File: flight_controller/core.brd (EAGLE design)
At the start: 94 x 90 mm, 116 parts, among them J1 MOLEX-2POS, J10 MOLEX-2POS, J11 MOLEX-2POS, J12 MOLEX-2POS, J13 MOLEX-3POS, J14 MOLEX-3POS, J15 MOLEX-4POS, J16 MOLEX-3POS, J17 MOLEX-3POS, J18 MOLEX-3POS, J19 MOLEX-3POS, J2 MOLEX-2POS, J20 MOLEX-4POS, J3 MOLEX-2POS, J4 MOLEX-2POS, J5 MOLEX-2POS, J6 MOLEX-2POS, J7 MOLEX-2POS, J8 MOLEX-2POS, J9 MOLEX-2POS, Q1 MMBT2222A, Q14 MMBT2222A, Q15 MMBT2222A, Q16 MMBT2222A, Q17 MMBT2222A, Q3 MMBT2222A, Q4 MMBT2222A, Q9 MMBT2222A, U1 MPU-6000QFN-24, U2 MEAS-MS5611, U3 USD-SOCKETNEW, U4 STM32F405, U5 MIC5219 3.3V

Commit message: Replace XBee headers with SMD variant.
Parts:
- removed XB1: XBEE-PRO, maxstream:XBEE-PRO
- added U$1: XBEE-1B3, SparkFun-RF:XBEE-SMD
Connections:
- net 3.3V: now also U$1.1; no longer XB1.1
- net GND: now also U$1.10; no longer XB1.10
- net KILL: now also U$1.20; no longer XB1.20
- net RSSI: now also U$1.6; no longer XB1.6
- net RST: now also U$1.5; no longer XB1.5
- net UART6-RX: now also U$1.2; no longer XB1.2
- net UART6-TX: now also U$1.3; no longer XB1.3
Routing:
- net RSSI: track 27.9 -> 0.00 mm, vias 2 -> 0
- net RST: track 10.6 -> 0.00 mm
- net KILL: track 1.00 -> 0.00 mm
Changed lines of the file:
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@@
 </autorouter>
 <elements>
-<element name="XB1" library="maxstream" package="XBEE-PRO" value="XBEE-PRO" x="34.9" y="16.1" rot="R180">
-<attribute name="OC_NEWARK" value="42M2667" x="34.9" y="16.1" size="1.778" layer="27" rot="R180" display="off"/>
-<attribute name="MPN" value="XBP24-AWI-001" x="34.9" y="16.1" size="1.778" layer="27" rot="R180" display="off"/>
-<attribute name="MF" value="" x="34.9" y="16.1" size="1.778" layer="27" rot="R180" display="off"/>
-<attribute name="OC_FARNELL" value="1337916" x="34.9" y="16.1" size="1.778" layer="27" rot="R180" display="off"/>
-</element>
 <element name="U3" library="SparkFun-Connectors" package="MICRO-SD-SOCKET-PP" value="USD-SOCKETNEW" x="-0.5" y="-145.6">
 <attribute name="PROD_ID" value="CONN-07820" x="-0.5" y="-145.6" size="1.778" layer="27" display="off"/>
@@
 <element name="C16" library="SparkFun-Capacitors" package="0603-CAP" value="18pF" x="-187.5" y="-506.7">
 <attribute name="PROD_ID" value="CAP-08267" x="-187.5" y="-506.7" size="1.778" layer="27" display="off"/>
+</element>
+<element name="U$1" library="SparkFun-RF" package="XBEE-SMD" value="XBEE-1B3" x="-202.6" y="-501.9">
+<attribute name="PROD_ID" value="CONN-09042" x="-202.6" y="-501.9" size="1.778" layer="27" display="off"/>
 </element>
 </elements>
@@
 <via x="33" y="41" extent="1-16" drill="0.381"/>
 <wire x1="35.7" y1="36.5" x2="35.7" y2="36.6" width="0.8128" layer="1"/>
-<contactref element="XB1" pad="10"/>
 <contactref element="U4" pad="18"/>
 <contactref element="U4" pad="63"/>
@@
 <contactref element="C15" pad="2"/>
 <contactref element="C16" pad="2"/>
+<contactref element="U$1" pad="10"/>
 <wire x1="-127.4" y1="-372.6" x2="-136" y2="-372.6" width="0" layer="19" extent="1-1"/>
 <wire x1="-120.8" y1="-372.6" x2="-127.4" y2="-372.6" width="0" layer="19" extent="1-1"/>
@@
 <wire x1="-186.65" y1="-503.7" x2="-186.65" y2="-496.4" width="0" layer="19" extent="1-1"/>
 <wire x1="-186.65" y1="-506.7" x2="-186.65" y2="-503.7" width="0" layer="19" extent="1-1"/>
+<wire x1="-212.1" y1="-499.9" x2="-186.65" y2="-496.4" width="0" layer="19" extent="1-1"/>
 <wire x1="-36.2" y1="-212.723" x2="-41.25" y2="-287.7" width="0" layer="19" extent="1-1"/>
 <wire x1="-33.3" y1="-212.723" x2="-36.2" y2="-212.723" width="0" layer="19" extent="1-1"/>
@@
 <wire x1="-14.1" y1="-131.05" x2="-3.94" y2="-134.7" width="0" layer="19" extent="1-1"/>
 <wire x1="44.2" y1="2.1" x2="-0.95" y2="-132.05" width="0" layer="19" extent="1-1"/>
-<wire x1="45.9" y1="25.1" x2="44.2" y2="2.1" width="0" layer="19" extent="1-1"/>
-<wire x1="35.7" y1="36.5" x2="45.9" y2="25.1" width="0" layer="19" extent="1-1"/>
+<wire x1="35.7" y1="36.5" x2="44.2" y2="2.1" width="0" layer="19" extent="1-1"/>
 <wire x1="33" y1="41" x2="35.7" y2="36.6" width="0" layer="19" extent="1-1"/>
 <wire x1="31" y1="41" x2="33" y2="41" width="0" layer="19" extent="1-1"/>
@@
 </signal>
 <signal name="RST">
-<contactref element="XB1" pad="5"/>
-<wire x1="45.9" y1="15.1" x2="47.4" y2="15.1" width="0.254" layer="1"/>
-<wire x1="47.4" y1="15.1" x2="47.7" y2="14.8" width="0.254" layer="1"/>
-<wire x1="47.7" y1="14.8" x2="47.7" y2="10.2" width="0.254" layer="1"/>
-<wire x1="47.7" y1="10.2" x2="49.4" y2="8.5" width="0.254" layer="1"/>
-<wire x1="49.4" y1="8.5" x2="51.1" y2="8.5" width="0.254" layer="1"/>
 <contactref element="S1" pad="1"/>
 <contactref element="R8" pad="1"/>
 <contactref element="J20" pad="1"/>
+<contactref element="U$1" pad="5"/>
 <wire x1="-42.794" y1="-359.895" x2="-14.15" y2="-182.7" width="0" layer="19" extent="1-1"/>
 <wire x1="-183" y1="-382.5" x2="-42.794" y2="-359.895" width="0" layer="19" extent="1-1"/>
-<wire x1="49.4" y1="8.5" x2="-14.15" y2="-182.7" width="0" layer="19" extent="1-1"/>
+<wire x1="-215.1" y1="-489.9" x2="-183" y2="-382.5" width="0" layer="19" extent="1-1"/>
 </signal>
 <signal name="PA12">
@@
 </signal>
 <signal name="3.3V">
-<contactref element="XB1" pad="1"/>
 <contactref element="U4" pad="1"/>
 <contactref element="U4" pad="19"/>
@@
 <contactref element="U4" pad="64"/>
 <contactref element="C9" pad="1"/>
+<contactref element="U$1" pad="1"/>
 <wire x1="-138" y1="-372.6" x2="-129.4" y2="-372.6" width="0" layer="19" extent="1-1"/>
 <wire x1="-180.7138" y1="-413.9967" x2="-138" y2="-372.6" width="0" layer="19" extent="1-1"/>
@@
 <wire x1="-186.65" y1="-475.4" x2="-188.35" y2="-466.4" width="0" layer="19" extent="1-1"/>
 <wire x1="-186.65" y1="-478.4" x2="-186.65" y2="-475.4" width="0" layer="19" extent="1-1"/>
+<wire x1="-215.1" y1="-481.9" x2="-186.65" y2="-478.4" width="0" layer="19" extent="1-1"/>
 <wire x1="-41.35" y1="-358.1" x2="-129.4" y2="-372.6" width="0" layer="19" extent="1-1"/>
 <wire x1="-33.75" y1="-222.5" x2="-41.35" y2="-358.1" width="0" layer="19" extent="1-1"/>
@@
 <wire x1="-1.7" y1="-161.9" x2="-8.2" y2="-161.9" width="0" layer="19" extent="1-1"/>
 <wire x1="0.5" y1="-152.2" x2="-9.2" y2="-150" width="0" layer="19" extent="1-1"/>
-<wire x1="45.9" y1="7.1" x2="0.5" y2="-152.2" width="0" layer="19" extent="1-1"/>
 </signal>
 <signal name="KILL">
-<contactref element="XB1" pad="20"/>
-<wire x1="22.9" y1="7.1" x2="23.9" y2="7.1" width="0.3048" layer="1"/>
 <contactref element="R28" pad="1"/>
 <contactref element="R11" pad="1"/>
 <contactref element="R13" pad="2"/>
-<wire x1="22.9" y1="7.1" x2="-27.55" y2="-219.5" width="0" layer="19" extent="1-1"/>
+<contactref element="U$1" pad="20"/>
 <wire x1="-184.75" y1="-435.8" x2="-27.55" y2="-219.5" width="0" layer="19" extent="1-1"/>
 <wire x1="-183.05" y1="-438.8" x2="-184.75" y2="-435.8" width="0" layer="19" extent="1-1"/>
+<wire x1="-193.1" y1="-481.9" x2="-183.05" y2="-438.8" width="0" layer="19" extent="1-1"/>
 </signal>
 <signal name="RSSI">
-<contactref element="XB1" pad="6"/>
-<wire x1="45.9" y1="17.1" x2="43.7" y2="17.1" width="0.254" layer="1"/>
-<wire x1="43.7" y1="17.1" x2="42.9" y2="16.3" width="0.254" layer="1"/>
-<via x="42.9" y="16.3" extent="1-16" drill="0.6"/>
-<wire x1="42.9" y1="16.3" x2="38.7" y2="16.3" width="0.254" layer="16"/>
-<wire x1="38.7" y1="16.3" x2="24.3" y2="1.9" width="0.254" layer="16"/>
-<via x="24.3" y="1.9" extent="1-16" drill="0.6"/>
 <contactref element="R27" pad="1"/>
-<wire x1="24.3" y1="1.9" x2="-30.65" y2="-219.5" width="0" layer="19" extent="1-16"/>
+<contactref element="U$1" pad="6"/>
+<wire x1="-212.1" y1="-491.9" x2="-30.65" y2="-219.5" width="0" layer="19" extent="1-1"/>
 </signal>
 <signal name="N$10">
@@
 </signal>
 <signal name="UART6-TX">
-<contactref element="XB1" pad="3"/>
 <contactref element="U4" pad="37"/>
 <contactref element="R29" pad="1"/>
 <contactref element="J19" pad="1"/>
+<contactref element="U$1" pad="3"/>
 <wire x1="0.5" y1="-157.7" x2="-24.45" y2="-219.5" width="0" layer="19" extent="1-1"/>
-<wire x1="45.9" y1="11.1" x2="0.5" y2="-157.7" width="0" layer="19" extent="1-1"/>
 <wire x1="-183" y1="-372.6" x2="-24.45" y2="-219.5" width="0" layer="19" extent="1-1"/>
+<wire x1="-215.1" y1="-485.9" x2="-183" y2="-372.6" width="0" layer="19" extent="1-1"/>
 </signal>
 <signal name="UART6-RX">
-<contactref element="XB1" pad="2"/>
 <contactref element="U4" pad="38"/>
 <contactref element="R30" pad="1"/>
 <contactref element="J19" pad="2"/>
-<wire x1="-36.85" y1="-222.5" x2="0.5" y2="-157.2" width="0" layer="19" extent="1-1"/>
-<wire x1="45.9" y1="9.1" x2="0.5" y2="-157.2" width="0" layer="19" extent="1-1"/>
-<wire x1="-181" y1="-372.6" x2="-36.85" y2="-222.5" width="0" layer="19" extent="1-1"/>
+<contactref element="U$1" pad="2"/>
+<wire x1="-181" y1="-372.6" x2="-212.1" y2="-483.9" width="0" layer="19" extent="1-1"/>
+<wire x1="-36.85" y1="-222.5" x2="-181" y2="-372.6" width="0" layer="19" extent="1-1"/>
+<wire x1="0.5" y1="-157.2" x2="-36.85" y2="-222.5" width="0" layer="19" extent="1-1"/>
 </signal>
 <signal name="ADC2">

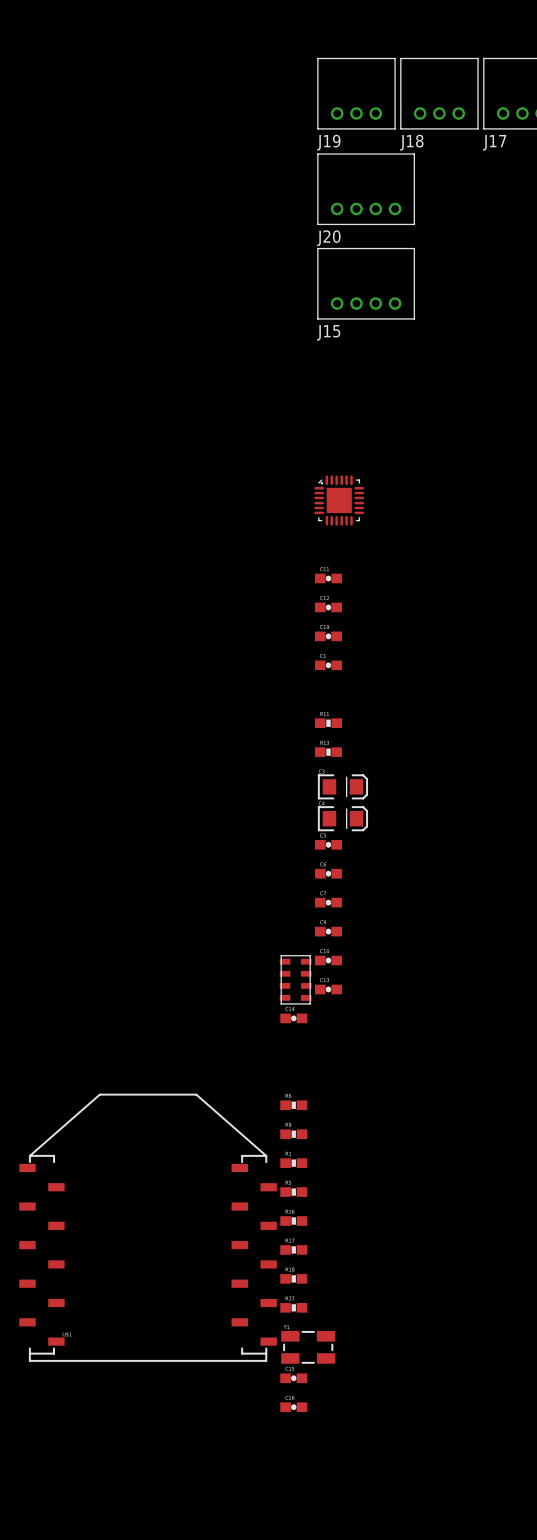
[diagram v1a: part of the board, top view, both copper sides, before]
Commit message: Reassign and rename UART buses to XBee and GPS.
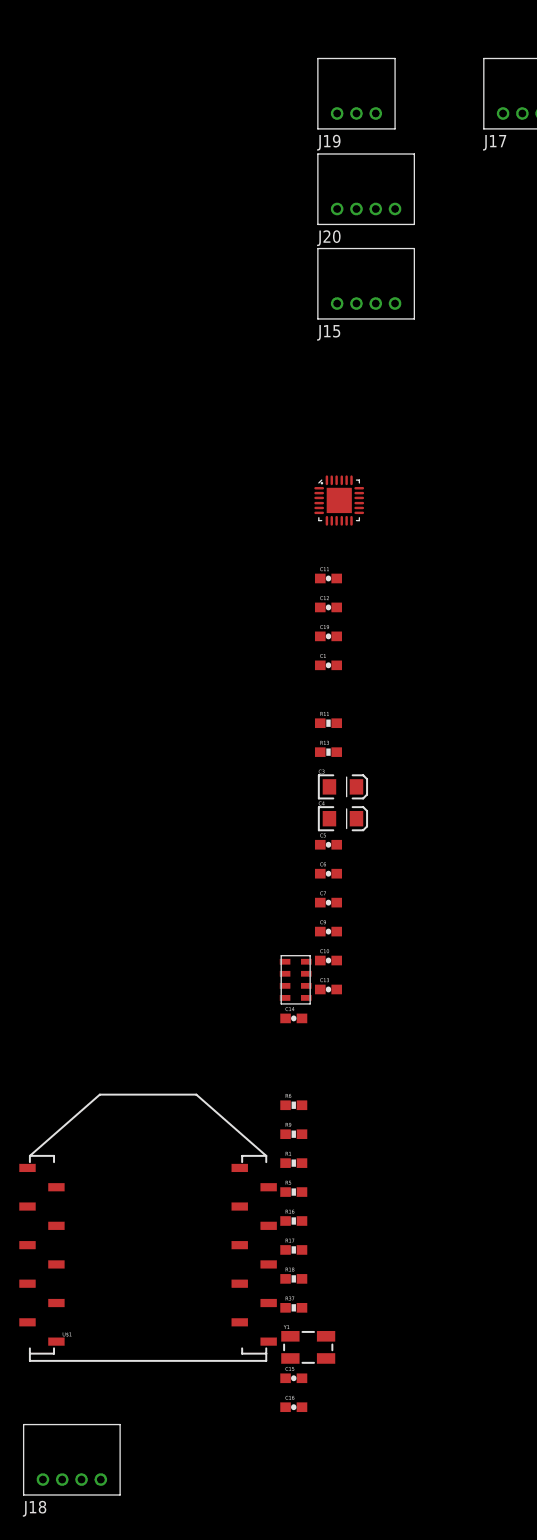
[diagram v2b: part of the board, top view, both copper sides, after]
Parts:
- J18: value MOLEX-3POS -> MOLEX-4POS; device aerial:MOLEX-2MM-MICROLATCH-3POS-RA -> aerial:MOLEX-2MM-MICROLATCH-4POS-RA
- moved J18 146.9 mm to (-213.5, -514.2)
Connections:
- removed net UART2-RX: J17.2, U4.17
- removed net UART2-TX: J17.1, U4.16
- removed net UART6-RX: J19.2, R30.1, U$1.2, U4.38
- removed net UART6-TX: J19.1, R29.1, U$1.3, U4.37
- new net SPISS-UNUSED: U4.4
- new net UART2-RX-XBEE: J17.2, R30.1, U$1.2, U4.17
- new net UART2-TX-XBEE: J17.1, R29.1, U$1.3, U4.16
- new net UART6-RX-GPS: J18.3, U4.38
- new net UART6-TX-GPS: J18.2, U4.37
- net 5V: now also J18.1
- net GND: now also J18.4, R13.1; no longer J18.3, R11.2
- net KILL-BASE: now also R11.2; no longer R13.1
- net RST: now also U4.7
- net UART4-RX: now also J19.2; no longer J18.2
- net UART4-TX: now also J19.1; no longer J18.1
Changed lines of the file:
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@@
 <element name="J16" library="aerial" package="MOLEX-2MM-MICROLATCH-3POS-RA" value="MOLEX-3POS" x="-157.2" y="-372.6"/>
 <element name="J17" library="aerial" package="MOLEX-2MM-MICROLATCH-3POS-RA" value="MOLEX-3POS" x="-165.8" y="-372.6"/>
-<element name="J18" library="aerial" package="MOLEX-2MM-MICROLATCH-3POS-RA" value="MOLEX-3POS" x="-174.4" y="-372.6"/>
 <element name="J19" library="aerial" package="MOLEX-2MM-MICROLATCH-3POS-RA" value="MOLEX-3POS" x="-183" y="-372.6"/>
 <element name="J20" library="aerial" package="MOLEX-2MM-MICROLATCH-4POS-RA" value="MOLEX-4POS" x="-183" y="-382.5"/>
@@
 <attribute name="PROD_ID" value="CONN-09042" x="-202.6" y="-501.9" size="1.778" layer="27" display="off"/>
 </element>
+<element name="J18" library="aerial" package="MOLEX-2MM-MICROLATCH-4POS-RA" value="MOLEX-4POS" x="-213.5" y="-514.2"/>
 </elements>
 <signals>
@@
 <contactref element="J14" pad="3"/>
 <contactref element="J17" pad="3"/>
-<contactref element="J18" pad="3"/>
 <contactref element="J19" pad="3"/>
 <contactref element="J20" pad="2"/>
@@
 <contactref element="C11" pad="2"/>
 <contactref element="C1" pad="2"/>
-<contactref element="R11" pad="2"/>
 <contactref element="C3" pad="C"/>
 <contactref element="C4" pad="C"/>
@@
 <contactref element="C16" pad="2"/>
 <contactref element="U$1" pad="10"/>
+<contactref element="J18" pad="4"/>
+<contactref element="R13" pad="1"/>
 <wire x1="-127.4" y1="-372.6" x2="-136" y2="-372.6" width="0" layer="19" extent="1-1"/>
 <wire x1="-120.8" y1="-372.6" x2="-127.4" y2="-372.6" width="0" layer="19" extent="1-1"/>
@@
 <wire x1="-153.2" y1="-372.6" x2="-136" y2="-372.6" width="0" layer="19" extent="1-1"/>
 <wire x1="-161.8" y1="-372.6" x2="-153.2" y2="-372.6" width="0" layer="19" extent="1-1"/>
-<wire x1="-170.4" y1="-372.6" x2="-161.8" y2="-372.6" width="0" layer="19" extent="1-1"/>
-<wire x1="-179" y1="-372.6" x2="-170.4" y2="-372.6" width="0" layer="19" extent="1-1"/>
+<wire x1="-179" y1="-372.6" x2="-161.8" y2="-372.6" width="0" layer="19" extent="1-1"/>
 <wire x1="-181" y1="-382.5" x2="-179" y2="-372.6" width="0" layer="19" extent="1-1"/>
 <wire x1="-177" y1="-392.3" x2="-181" y2="-382.5" width="0" layer="19" extent="1-1"/>
@@
 <wire x1="-183.05" y1="-426.8" x2="-183.05" y2="-423.8" width="0" layer="19" extent="1-1"/>
 <wire x1="-183.05" y1="-429.8" x2="-183.05" y2="-426.8" width="0" layer="19" extent="1-1"/>
-<wire x1="-183.05" y1="-435.8" x2="-183.05" y2="-429.8" width="0" layer="19" extent="1-1"/>
-<wire x1="-183.8" y1="-442.4" x2="-183.05" y2="-435.8" width="0" layer="19" extent="1-1"/>
+<wire x1="-184.75" y1="-438.8" x2="-183.05" y2="-429.8" width="0" layer="19" extent="1-1"/>
+<wire x1="-183.8" y1="-442.4" x2="-184.75" y2="-438.8" width="0" layer="19" extent="1-1"/>
 <wire x1="-183.8" y1="-445.7" x2="-183.8" y2="-442.4" width="0" layer="19" extent="1-1"/>
 <wire x1="-183.05" y1="-448.4" x2="-183.8" y2="-445.7" width="0" layer="19" extent="1-1"/>
@@
 <wire x1="-186.65" y1="-503.7" x2="-186.65" y2="-496.4" width="0" layer="19" extent="1-1"/>
 <wire x1="-186.65" y1="-506.7" x2="-186.65" y2="-503.7" width="0" layer="19" extent="1-1"/>
-<wire x1="-212.1" y1="-499.9" x2="-186.65" y2="-496.4" width="0" layer="19" extent="1-1"/>
+<wire x1="-207.5" y1="-514.2" x2="-186.65" y2="-506.7" width="0" layer="19" extent="1-1"/>
+<wire x1="-212.1" y1="-499.9" x2="-207.5" y2="-514.2" width="0" layer="19" extent="1-1"/>
 <wire x1="-36.2" y1="-212.723" x2="-41.25" y2="-287.7" width="0" layer="19" extent="1-1"/>
 <wire x1="-33.3" y1="-212.723" x2="-36.2" y2="-212.723" width="0" layer="19" extent="1-1"/>
@@
 <contactref element="J20" pad="1"/>
 <contactref element="U$1" pad="5"/>
+<contactref element="U4" pad="7"/>
+<wire x1="-11.4" y1="-155.2" x2="-14.15" y2="-182.7" width="0" layer="19" extent="1-1"/>
 <wire x1="-42.794" y1="-359.895" x2="-14.15" y2="-182.7" width="0" layer="19" extent="1-1"/>
 <wire x1="-183" y1="-382.5" x2="-42.794" y2="-359.895" width="0" layer="19" extent="1-1"/>
@@
 <contactref element="JP1" pad="VBUS"/>
 <contactref element="C4" pad="A"/>
+<contactref element="J18" pad="1"/>
 <wire x1="-24.55" y1="-196.0001" x2="-30.65" y2="-222.5" width="0" layer="19" extent="1-1"/>
 <wire x1="-22.65" y1="-196.0001" x2="-24.55" y2="-196.0001" width="0" layer="19" extent="1-1"/>
 <wire x1="-40" y1="-350.45" x2="-30.65" y2="-222.5" width="0" layer="19" extent="1-1"/>
 <wire x1="-181" y1="-445.7" x2="-40" y2="-350.45" width="0" layer="19" extent="1-1"/>
+<wire x1="-213.5" y1="-514.2" x2="-181" y2="-445.7" width="0" layer="19" extent="1-1"/>
 </signal>
 <signal name="ADC1-IN">
@@
 <signal name="UART4-TX">
 <contactref element="U4" pad="14"/>
-<contactref element="J18" pad="1"/>
-<wire x1="-174.4" y1="-372.6" x2="-11.4" y2="-158.7" width="0" layer="19" extent="1-1"/>
+<contactref element="J19" pad="1"/>
+<wire x1="-183" y1="-372.6" x2="-11.4" y2="-158.7" width="0" layer="19" extent="1-1"/>
 </signal>
 <signal name="UART4-RX">
 <contactref element="U4" pad="15"/>
-<contactref element="J18" pad="2"/>
-<wire x1="-172.4" y1="-372.6" x2="-11.4" y2="-159.2" width="0" layer="19" extent="1-1"/>
-</signal>
-<signal name="UART2-TX">
-<contactref element="U4" pad="16"/>
-<contactref element="J17" pad="1"/>
-<wire x1="-165.8" y1="-372.6" x2="-11.4" y2="-159.7" width="0" layer="19" extent="1-1"/>
-</signal>
-<signal name="UART2-RX">
-<contactref element="U4" pad="17"/>
-<contactref element="J17" pad="2"/>
-<wire x1="-163.8" y1="-372.6" x2="-9.2" y2="-161.9" width="0" layer="19" extent="1-1"/>
+<contactref element="J19" pad="2"/>
+<wire x1="-181" y1="-372.6" x2="-11.4" y2="-159.2" width="0" layer="19" extent="1-1"/>
 </signal>
 <signal name="TIM3-CH3">
@@
 <contactref element="J20" pad="4"/>
 <wire x1="-177" y1="-382.5" x2="-1.7" y2="-150" width="0" layer="19" extent="1-1"/>
-</signal>
-<signal name="UART6-TX">
-<contactref element="U4" pad="37"/>
-<contactref element="R29" pad="1"/>
-<contactref element="J19" pad="1"/>
-<contactref element="U$1" pad="3"/>
-<wire x1="0.5" y1="-157.7" x2="-24.45" y2="-219.5" width="0" layer="19" extent="1-1"/>
-<wire x1="-183" y1="-372.6" x2="-24.45" y2="-219.5" width="0" layer="19" extent="1-1"/>
-<wire x1="-215.1" y1="-485.9" x2="-183" y2="-372.6" width="0" layer="19" extent="1-1"/>
-</signal>
-<signal name="UART6-RX">
-<contactref element="U4" pad="38"/>
-<contactref element="R30" pad="1"/>
-<contactref element="J19" pad="2"/>
-<contactref element="U$1" pad="2"/>
-<wire x1="-181" y1="-372.6" x2="-212.1" y2="-483.9" width="0" layer="19" extent="1-1"/>
-<wire x1="-36.85" y1="-222.5" x2="-181" y2="-372.6" width="0" layer="19" extent="1-1"/>
-<wire x1="0.5" y1="-157.2" x2="-36.85" y2="-222.5" width="0" layer="19" extent="1-1"/>
 </signal>
 <signal name="ADC2">
@@
 <contactref element="Q15" pad="1"/>
 <contactref element="Q9" pad="1"/>
-<contactref element="R13" pad="1"/>
+<contactref element="R11" pad="2"/>
 <wire x1="-43.15" y1="-336.1" x2="-43.15" y2="-343" width="0" layer="19" extent="1-1"/>
 <wire x1="-43.15" y1="-329.2" x2="-43.15" y2="-336.1" width="0" layer="19" extent="1-1"/>
@@
 <wire x1="-43.15" y1="-301.6" x2="-43.15" y2="-308.5" width="0" layer="19" extent="1-1"/>
 <wire x1="-43.15" y1="-287.7" x2="-43.15" y2="-301.6" width="0" layer="19" extent="1-1"/>
-<wire x1="-184.75" y1="-438.8" x2="-43.15" y2="-343" width="0" layer="19" extent="1-1"/>
+<wire x1="-183.05" y1="-435.8" x2="-43.15" y2="-343" width="0" layer="19" extent="1-1"/>
 </signal>
 <signal name="N$1">
@@
 <wire x1="-182.5225" y1="-414.8216" x2="-184.75" y2="-423.8" width="0" layer="19" extent="1-1"/>
 </signal>
+<signal name="UART6-TX-GPS">
+<contactref element="U4" pad="37"/>
+<contactref element="J18" pad="2"/>
+<wire x1="0.5" y1="-157.7" x2="-211.5" y2="-514.2" width="0" layer="19" extent="1-1"/>
+</signal>
+<signal name="UART6-RX-GPS">
+<contactref element="U4" pad="38"/>
+<contactref element="J18" pad="3"/>
+<wire x1="0.5" y1="-157.2" x2="-209.5" y2="-514.2" width="0" layer="19" extent="1-1"/>
+</signal>
+<signal name="UART2-TX-XBEE">
+<contactref element="U4" pad="16"/>
+<contactref element="U$1" pad="3"/>
+<contactref element="J17" pad="1"/>
+<contactref element="R29" pad="1"/>
+<wire x1="-11.4" y1="-159.7" x2="-24.45" y2="-219.5" width="0" layer="19" extent="1-1"/>
+<wire x1="-165.8" y1="-372.6" x2="-24.45" y2="-219.5" width="0" layer="19" extent="1-1"/>
+<wire x1="-215.1" y1="-485.9" x2="-165.8" y2="-372.6" width="0" layer="19" extent="1-1"/>
+</signal>
+<signal name="UART2-RX-XBEE">
+<contactref element="U4" pad="17"/>
+<contactref element="U$1" pad="2"/>
+<contactref element="J17" pad="2"/>
+<contactref element="R30" pad="1"/>
+<wire x1="-163.8" y1="-372.6" x2="-212.1" y2="-483.9" width="0" layer="19" extent="1-1"/>
+<wire x1="-36.85" y1="-222.5" x2="-163.8" y2="-372.6" width="0" layer="19" extent="1-1"/>
+<wire x1="-9.2" y1="-161.9" x2="-36.85" y2="-222.5" width="0" layer="19" extent="1-1"/>
+</signal>
+<signal name="SPISS-UNUSED">
+<contactref element="U4" pad="4"/>
+</signal>
 </signals>
